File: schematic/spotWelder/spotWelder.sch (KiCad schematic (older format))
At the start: 33 parts, among them J1 InterBoard, Q1 Q_NPN_BCE, SW1 Rotary_Encoder_Switch, U1 GD32F1/F3/VF1 or STM32F1, U3 DC/DC converter

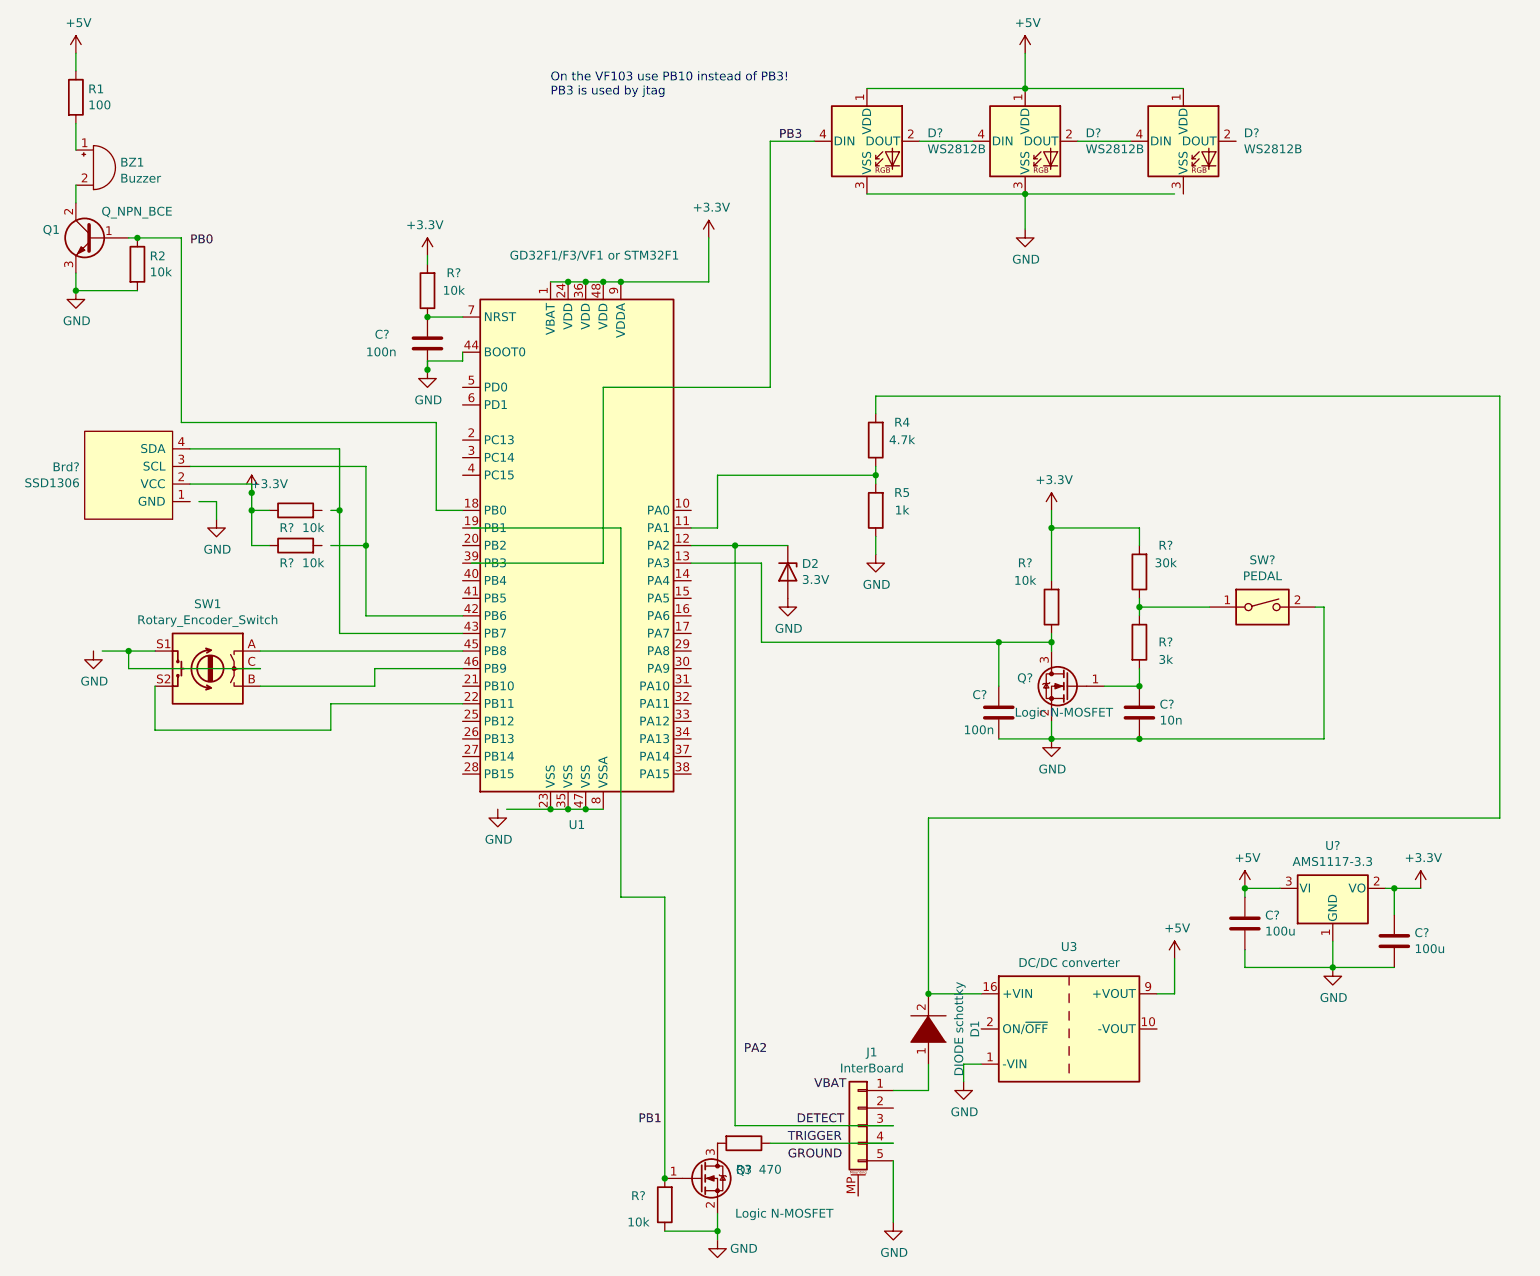
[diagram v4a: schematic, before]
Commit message: sync + update schematic with back EMF diode
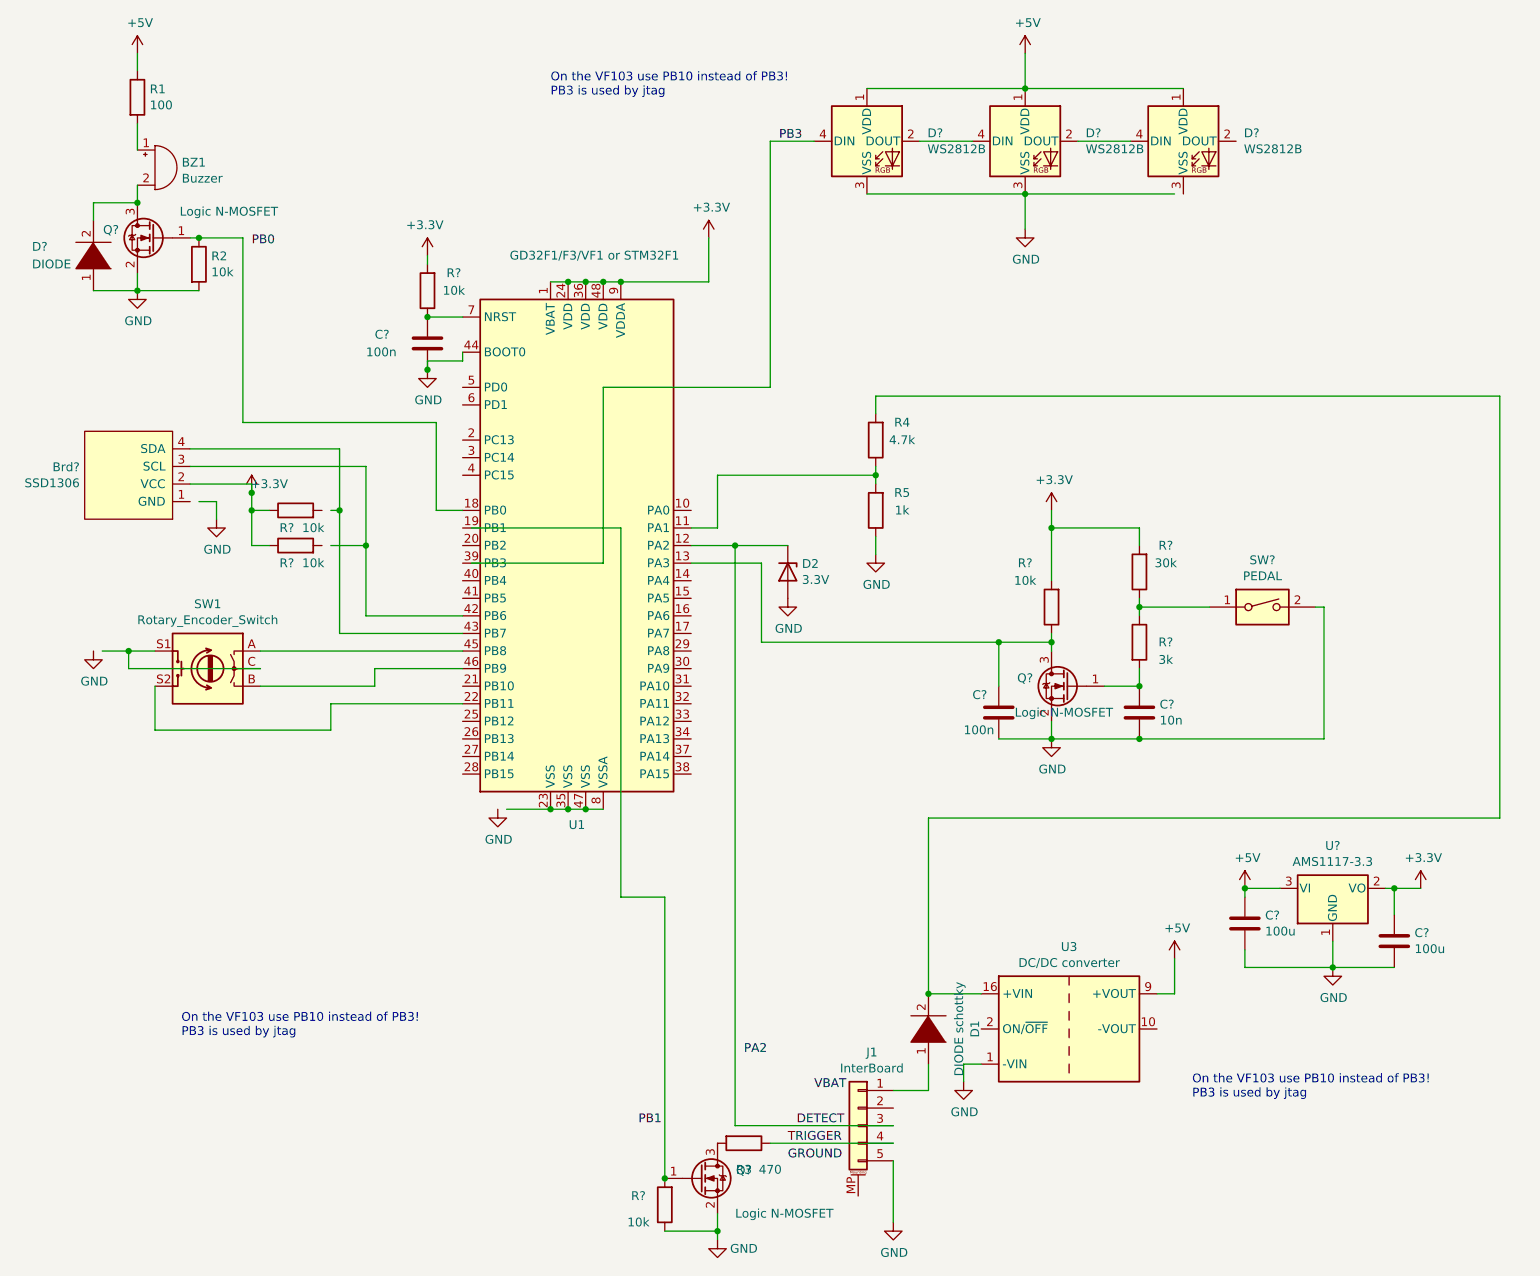
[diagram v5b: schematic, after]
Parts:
- removed Q1: Q_NPN_BCE, symbol Device:Q_NPN_BCE
- added D?: DIODE, symbol pspice:DIODE
- added Q?: Logic N-MOSFET, Package_TO_SOT_SMD:SOT-23, symbol Transistor_FET:ZXMN2A01F
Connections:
- wire segments 131 -> 134
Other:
- moved on the sheet: BZ1, R1, R2
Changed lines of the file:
@@
 L Device:Buzzer BZ1
 U 1 1 60584C9C
-P 900 1550
-F 0 "BZ1" H 1052 1579 50  0000 L CNN
-F 1 "Buzzer" H 1052 1488 50  0000 L CNN
-F 2 "" V 875 1650 50  0001 C CNN
-F 3 "~" V 875 1650 50  0001 C CNN
-	1    900  1550
+P 1250 1550
+F 0 "BZ1" H 1402 1579 50  0000 L CNN
+F 1 "Buzzer" H 1402 1488 50  0000 L CNN
+F 2 "" V 1225 1650 50  0001 C CNN
+F 3 "~" V 1225 1650 50  0001 C CNN
+	1    1250 1550
 	1    0    0    -1
 $EndComp
@@
 L power:GND #PWR02
 U 1 1 60585A6D
-P 800 2250
-F 0 "#PWR02" H 800 2000 50  0001 C CNN
-F 1 "GND" H 805 2077 50  0000 C CNN
-F 2 "" H 800 2250 50  0001 C CNN
-F 3 "" H 800 2250 50  0001 C CNN
-	1    800  2250
+P 1150 2250
+F 0 "#PWR02" H 1150 2000 50  0001 C CNN
+F 1 "GND" H 1155 2077 50  0000 C CNN
+F 2 "" H 1150 2250 50  0001 C CNN
+F 3 "" H 1150 2250 50  0001 C CNN
+	1    1150 2250
 	1    0    0    -1
 $EndComp
@@
 L Device:R R1
 U 1 1 605B195B
-P 800 1150
-F 0 "R1" H 870 1196 50  0000 L CNN
-F 1 "100" H 870 1105 50  0000 L CNN
-F 2 "" V 730 1150 50  0001 C CNN
-F 3 "~" H 800 1150 50  0001 C CNN
-	1    800  1150
+P 1150 1150
+F 0 "R1" H 1220 1196 50  0000 L CNN
+F 1 "100" H 1220 1105 50  0000 L CNN
+F 2 "" V 1080 1150 50  0001 C CNN
+F 3 "~" H 1150 1150 50  0001 C CNN
+	1    1150 1150
 	1    0    0    -1
 $EndComp
@@
 L power:+5V #PWR01
 U 1 1 605E35CF
-P 800 900
-F 0 "#PWR01" H 800 750 50  0001 C CNN
-F 1 "+5V" H 815 1073 50  0000 C CNN
-F 2 "" H 800 900 50  0001 C CNN
-F 3 "" H 800 900 50  0001 C CNN
-	1    800  900
+P 1150 900
+F 0 "#PWR01" H 1150 750 50  0001 C CNN
+F 1 "+5V" H 1165 1073 50  0000 C CNN
+F 2 "" H 1150 900 50  0001 C CNN
+F 3 "" H 1150 900 50  0001 C CNN
+	1    1150 900
 	1    0    0    -1
 $EndComp
@@
 L Device:R R2
 U 1 1 605F82FD
-P 1150 2100
-F 0 "R2" H 1220 2146 50  0000 L CNN
-F 1 "10k" H 1220 2055 50  0000 L CNN
-F 2 "" V 1080 2100 50  0001 C CNN
-F 3 "~" H 1150 2100 50  0001 C CNN
-	1    1150 2100
-	1    0    0    -1
-$EndComp
-Wire Wire Line
-	800  1000 800  900
-Wire Wire Line
-	800  1450 800  1300
-Wire Wire Line
-	800  1750 800  1650
-Wire Wire Line
-	1100 1950 1150 1950
-Wire Wire Line
-	1150 2250 800  2250
-Connection ~ 800  2250
-Wire Wire Line
-	800  2150 800  2250
-$Comp
-L Device:Q_NPN_BCE Q1
-U 1 1 60591CD0
-P 900 1950
-F 0 "Q1" H 1091 1996 50  0000 L CNN
-F 1 "Q_NPN_BCE" H 450 2100 50  0000 L CNN
-F 2 "" H 1100 2050 50  0001 C CNN
-F 3 "~" H 900 1950 50  0001 C CNN
-	1    900  1950
-	-1   0    0    -1
-$EndComp
+P 1500 2100
+F 0 "R2" H 1570 2146 50  0000 L CNN
+F 1 "10k" H 1570 2055 50  0000 L CNN
+F 2 "" V 1430 2100 50  0001 C CNN
+F 3 "~" H 1500 2100 50  0001 C CNN
+	1    1500 2100
+	1    0    0    -1
+$EndComp
+Wire Wire Line
+	1150 1000 1150 900
+Wire Wire Line
+	1150 1450 1150 1300
+Wire Wire Line
+	1150 1750 1150 1650
+Wire Wire Line
+	1450 1950 1500 1950
+Wire Wire Line
+	1500 2250 1150 2250
+Connection ~ 1150 2250
+Wire Wire Line
+	1150 2150 1150 2250
 $Comp
 L Transistor_FET:ZXMN2A01F Q?
@@
 Wire Wire Line
 	2250 4600 3000 4600
-Connection ~ 1150 1950
+Connection ~ 1500 1950
 Wire Wire Line
 	2850 3500 2850 3000
@@
 Connection ~ 7450 5650
 Wire Wire Line
-	2850 3000 1400 3000
-Wire Wire Line
-	1400 3000 1400 1950
-Wire Wire Line
-	1150 1950 1400 1950
+	2850 3000 1750 3000
+Wire Wire Line
+	1750 3000 1750 1950
+Wire Wire Line
+	1500 1950 1750 1950
 $Comp
 L power:+3.3V #PWR?
@@
 Wire Wire Line
 	4550 3700 4850 3700
-Text Label 1450 2000 0    50   ~ 0
+Text Label 1800 2000 0    50   ~ 0
 PB0
 Text Label 4600 6600 0    50   ~ 0
@@
 Text Notes 3500 1150 0    50   ~ 0
 On the VF103 use PB10 instead of PB3!\nPB3 is used by jtag
+$Comp
+L pspice:DIODE D?
+U 1 1 61881DDB
+P 900 2050
+F 0 "D?" V 950 1700 50  0000 L CNN
+F 1 "DIODE" V 850 1700 50  0000 L CNN
+F 2 "" H 900 2050 50  0001 C CNN
+F 3 "~" H 900 2050 50  0001 C CNN
+	1    900  2050
+	0    1    -1   0
+$EndComp
+$Comp
+L Transistor_FET:ZXMN2A01F Q?
+U 1 1 61886D67
+P 1250 1950
+F 0 "Q?" H 1455 1996 50  0000 L CNN
+F 1 "Logic N-MOSFET" H 550 2100 50  0000 L CNN
+F 2 "Package_TO_SOT_SMD:SOT-23" H 1450 1875 50  0001 L CIN
+F 3 "http://www.diodes.com/assets/Datasheets/ZXMN2A01F.pdf" H 1250 1950 50  0001 L CNN
+	1    1250 1950
+	-1   0    0    -1
+$EndComp
+Wire Wire Line
+	1150 1750 900  1750
+Wire Wire Line
+	900  1750 900  1850
+Connection ~ 1150 1750
+Wire Wire Line
+	900  2250 1150 2250
+Text Notes 7150 6850 0    50   ~ 0
+On the VF103 use PB10 instead of PB3!\nPB3 is used by jtag
+Text Notes 1400 6500 0    50   ~ 0
+On the VF103 use PB10 instead of PB3!\nPB3 is used by jtag
 $EndSCHEMATC
